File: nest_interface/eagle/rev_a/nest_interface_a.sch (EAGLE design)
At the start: 113 parts, among them J1 MOLEX_MICRO_USB_B_047346, J10 CONN_BLOCK_2, J11 CONN_BLOCK_2, J12 CONN_BLOCK_2, J13 CONN_BLOCK_2, J14 CONN_BLOCK_3, J15 CONN_BLOCK_3, J16 CONN_BLOCK_7, J17 CONN_BLOCK_7, J18 CONN_BLOCK_8, J19 CONN_BLOCK_8, J2 MOLEX_MICRO_USB_B_047346, J20 CONN_BLOCK_8, J21 CONN_BLOCK_8, J5 PJ-036A-SMT, J6 CONN_BLOCK_2, J7 CONN_BLOCK_2, J8 CONN_BLOCK_2, J9 CONN_BLOCK_2, U1 EPIC-CORE_A, U2 MSP430F1611IPM, U3 FT232RL, U4 FT232RL, U5 MPC1825, U6 TC1262, U7 PCA9575, U8 PCA9575, Y1 FC-135_32.768KA-A3

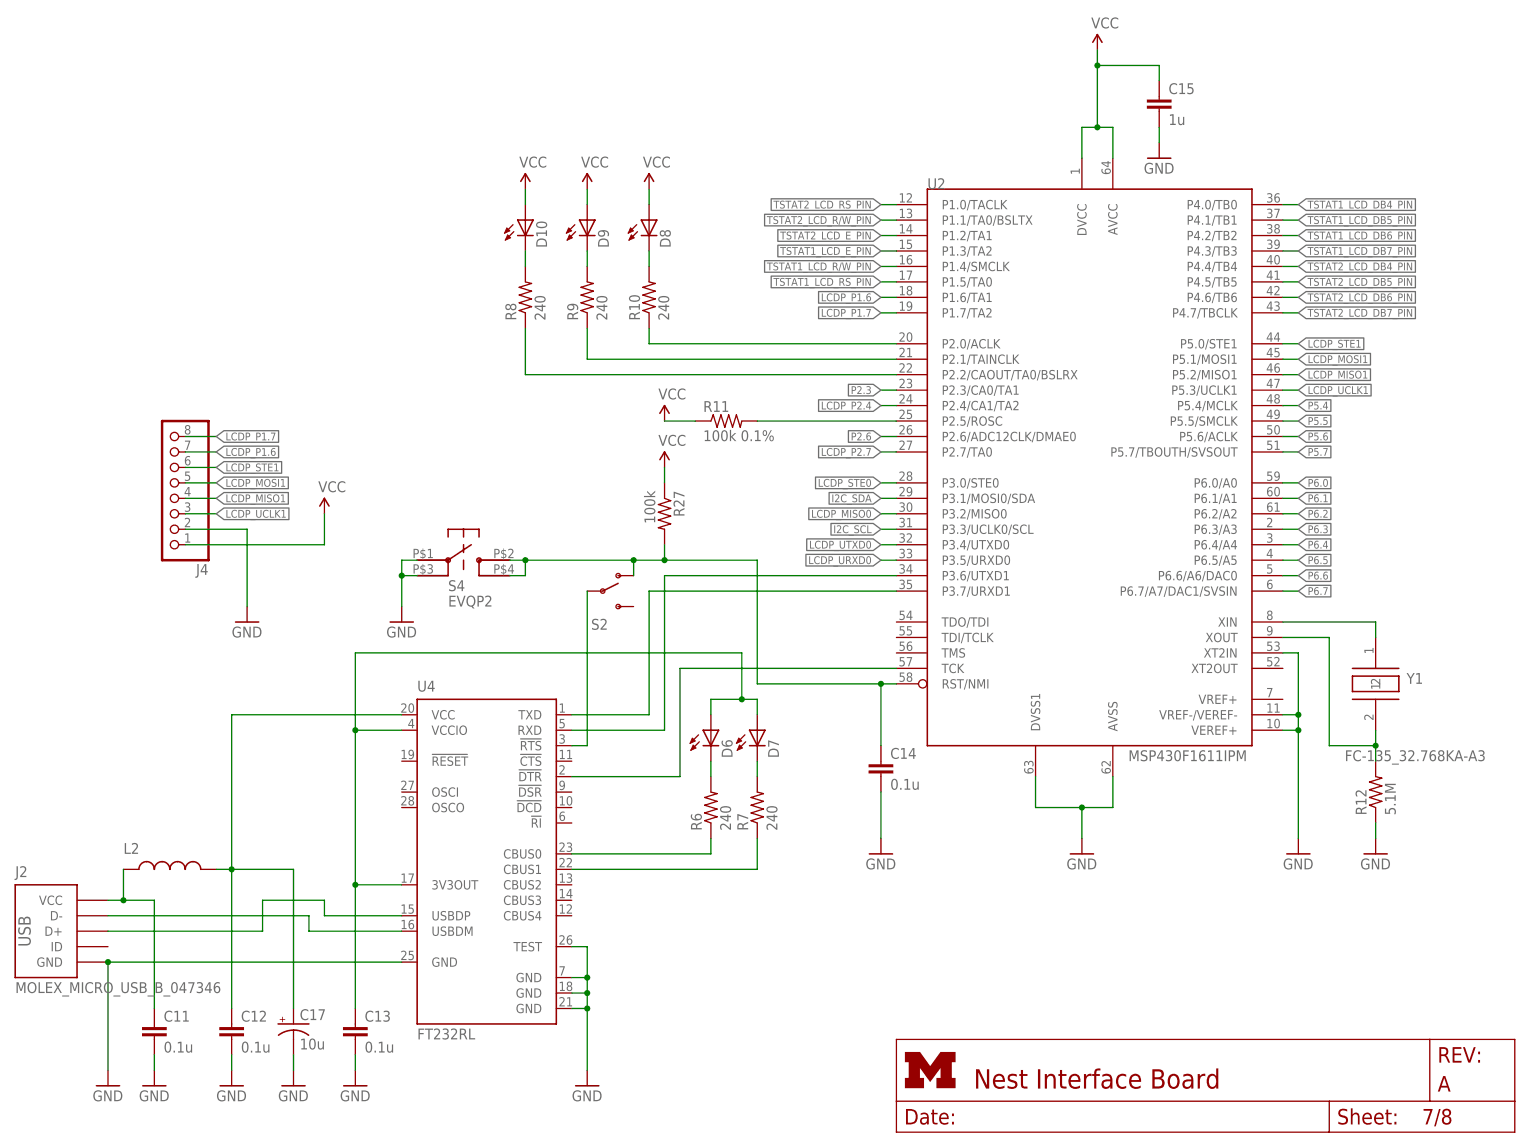
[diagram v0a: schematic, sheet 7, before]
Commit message: added board for keypad socket
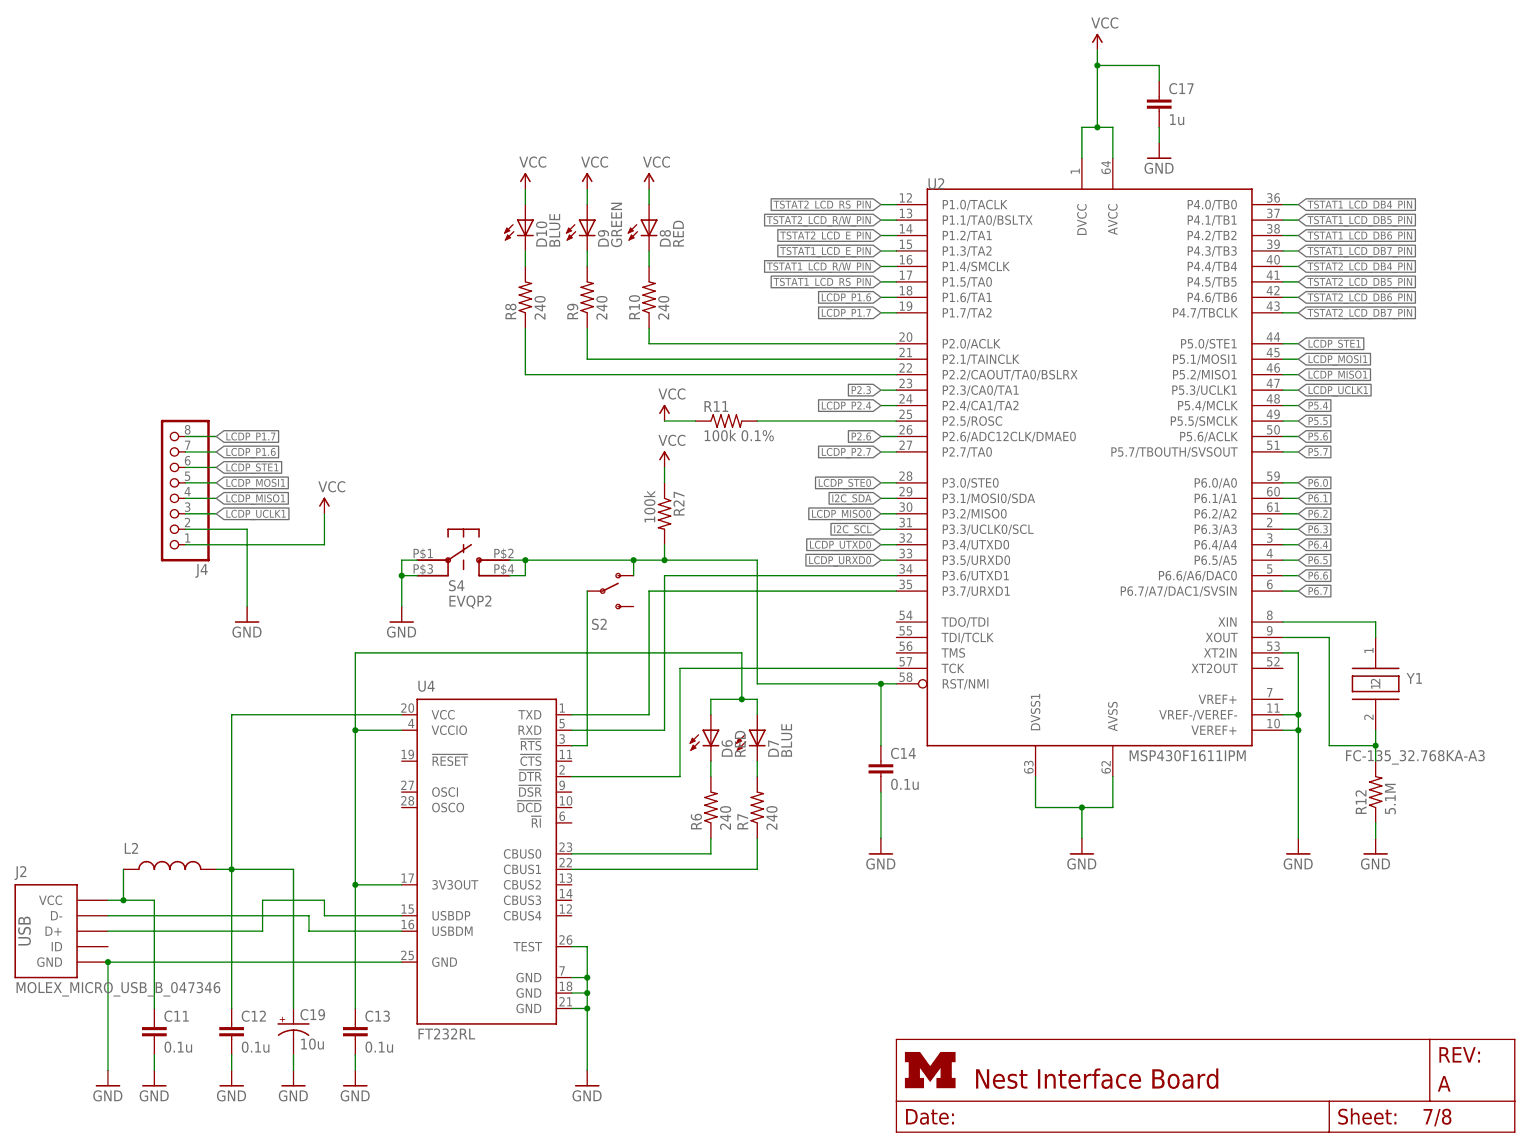
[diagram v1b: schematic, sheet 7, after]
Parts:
- C15: value 1u -> 0.1u
- C16: value 10u -> 0.1u; device SparkFun:CAP_POL1206 -> rcl:C-EUC0603
- C17: value 10u -> 1u; device SparkFun:CAP_POL1206 -> rcl:C-EUC0603
- C18, C19: value 0.1u -> 10u; device rcl:C-EUC0603 -> SparkFun:CAP_POL1206; DIGIKEY (none) -> 478-1655-1-ND
- D1, D3, D6, D8: value (none) -> RED
- D10, D2, D5, D7: value (none) -> BLUE
- D4, D9: value (none) -> GREEN
- L1: DIGIKEY (none) -> 240-2373-1-ND
- S3, S4: DIGIKEY (none) -> P11084SCT-ND
- Y1: DIGIKEY (none) -> 535-9543-1-ND
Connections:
- net GND: now also C16.2, C17.2, C18.-, C19.-; no longer C16.-, C17.-, C18.2, C19.2
- net N$43: now also C19.+; no longer C17.+
- net N$6: now also C18.+; no longer C16.+
- net VCC: now also C16.1, C17.1; no longer C18.1, C19.1

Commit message: nest
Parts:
- removed J4: (no value), pinhead:PINHD-1X8
- added JP1: (no value), pinhead:PINHD-1X10
- added U$1: UMICH_SOLID_LARGE, nest_interface:UMICH_SOLID_LARGE
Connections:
- net P2.3 renamed LCDP_P2.3
- removed net P5.4: U2.P5.4/MCLK
- new net LCDP_P5.4: JP1.2, U2.P5.4/MCLK
- net GND: now also JP1.10; no longer J4.2
- net LCDP_MISO1: now also JP1.5; no longer J4.4
- net LCDP_MOSI1: now also JP1.6; no longer J4.5
- net LCDP_P1.6: now also JP1.8; no longer J4.7
- net LCDP_P1.7: now also JP1.9; no longer J4.8
- net LCDP_P2.4: now also JP1.3
- net LCDP_STE1: now also JP1.7; no longer J4.6
- net LCDP_UCLK1: now also JP1.4; no longer J4.3
- net VCC: now also JP1.1; no longer J4.1
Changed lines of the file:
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@@
 <part name="FRAME7" library="nest_interface" deviceset="LETTER_L" device=""/>
 <part name="FRAME8" library="nest_interface" deviceset="LETTER_L" device=""/>
-<part name="J4" library="pinhead" deviceset="PINHD-1X8" device=""/>
 <part name="GND19" library="supply1" deviceset="GND" device=""/>
 <part name="P+17" library="SparkFun" deviceset="VCC" device=""/>
@@
 <part name="C16" library="rcl" deviceset="C-EU" device="C0603" value="0.1u"/>
 <part name="GND27" library="supply1" deviceset="GND" device=""/>
+<part name="JP1" library="pinhead" deviceset="PINHD-1X10" device=""/>
+<part name="U$1" library="nest_interface" deviceset="UMICH_SOLID" device="_LARGE"/>
 </parts>
 <sheets>
@@
 <instance part="FRAME1" gate="G$1" x="0" y="0"/>
 <instance part="FRAME1" gate="G$2" x="147.32" y="0"/>
+<instance part="U$1" gate="G$1" x="116.84" y="170.18"/>
 </instances>
 <busses>
@@
 <instance part="FRAME7" gate="G$1" x="0" y="0"/>
 <instance part="FRAME7" gate="G$2" x="147.32" y="0"/>
-<instance part="J4" gate="A" x="27.94" y="106.68" rot="R180"/>
-<instance part="GND19" gate="1" x="40.64" y="83.82"/>
-<instance part="P+17" gate="1" x="53.34" y="101.6"/>
+<instance part="GND19" gate="1" x="38.1" y="121.92"/>
+<instance part="P+17" gate="1" x="38.1" y="152.4"/>
+<instance part="JP1" gate="A" x="27.94" y="139.7" rot="MR0"/>
 </instances>
 <busses>
@@
 </segment>
 <segment>
-<pinref part="J4" gate="A" pin="1"/>
-<wire x1="30.48" y1="96.52" x2="53.34" y2="96.52" width="0.1524" layer="91"/>
-<wire x1="53.34" y1="96.52" x2="53.34" y2="101.6" width="0.1524" layer="91"/>
+<pinref part="JP1" gate="A" pin="1"/>
+<wire x1="30.48" y1="149.86" x2="38.1" y2="149.86" width="0.1524" layer="91"/>
 <pinref part="P+17" gate="1" pin="VCC"/>
+<wire x1="38.1" y1="149.86" x2="38.1" y2="152.4" width="0.1524" layer="91"/>
 </segment>
 </net>
@@
 </segment>
 <segment>
-<pinref part="J4" gate="A" pin="2"/>
-<wire x1="30.48" y1="99.06" x2="40.64" y2="99.06" width="0.1524" layer="91"/>
-<wire x1="40.64" y1="99.06" x2="40.64" y2="86.36" width="0.1524" layer="91"/>
+<pinref part="JP1" gate="A" pin="10"/>
+<wire x1="30.48" y1="127" x2="38.1" y2="127" width="0.1524" layer="91"/>
 <pinref part="GND19" gate="1" pin="GND"/>
+<wire x1="38.1" y1="127" x2="38.1" y2="124.46" width="0.1524" layer="91"/>
 </segment>
 </net>
@@
 </segment>
 <segment>
-<pinref part="J4" gate="A" pin="6"/>
-<wire x1="30.48" y1="109.22" x2="35.56" y2="109.22" width="0.1524" layer="91"/>
-<label x="35.56" y="109.22" size="1.27" layer="95" xref="yes"/>
+<pinref part="JP1" gate="A" pin="7"/>
+<wire x1="30.48" y1="134.62" x2="35.56" y2="134.62" width="0.1524" layer="91"/>
+<label x="35.56" y="134.62" size="1.27" layer="95" xref="yes"/>
 </segment>
 </net>
@@
 </segment>
 <segment>
-<pinref part="J4" gate="A" pin="5"/>
-<wire x1="30.48" y1="106.68" x2="35.56" y2="106.68" width="0.1524" layer="91"/>
-<label x="35.56" y="106.68" size="1.27" layer="95" xref="yes"/>
+<pinref part="JP1" gate="A" pin="6"/>
+<wire x1="30.48" y1="137.16" x2="35.56" y2="137.16" width="0.1524" layer="91"/>
+<label x="35.56" y="137.16" size="1.27" layer="95" xref="yes"/>
 </segment>
 </net>
@@
 </segment>
 <segment>
-<pinref part="J4" gate="A" pin="4"/>
-<wire x1="30.48" y1="104.14" x2="35.56" y2="104.14" width="0.1524" layer="91"/>
-<label x="35.56" y="104.14" size="1.27" layer="95" xref="yes"/>
+<pinref part="JP1" gate="A" pin="5"/>
+<wire x1="30.48" y1="139.7" x2="35.56" y2="139.7" width="0.1524" layer="91"/>
+<label x="35.56" y="139.7" size="1.27" layer="95" xref="yes"/>
 </segment>
 </net>
@@
 </segment>
 <segment>
-<pinref part="J4" gate="A" pin="3"/>
-<wire x1="30.48" y1="101.6" x2="35.56" y2="101.6" width="0.1524" layer="91"/>
-<label x="35.56" y="101.6" size="1.27" layer="95" xref="yes"/>
+<pinref part="JP1" gate="A" pin="4"/>
+<wire x1="30.48" y1="142.24" x2="35.56" y2="142.24" width="0.1524" layer="91"/>
+<label x="35.56" y="142.24" size="1.27" layer="95" xref="yes"/>
 </segment>
 </net>
-<net name="P5.4" class="0">
+<net name="LCDP_P5.4" class="0">
 <segment>
 <pinref part="U2" gate="G$1" pin="P5.4/MCLK"/>
@@
 <label x="213.36" y="119.38" size="1.27" layer="95" xref="yes"/>
 </segment>
+<segment>
+<pinref part="JP1" gate="A" pin="2"/>
+<wire x1="30.48" y1="147.32" x2="35.56" y2="147.32" width="0.1524" layer="91"/>
+<label x="35.56" y="147.32" size="1.27" layer="95" xref="yes"/>
+</segment>
 </net>
 <net name="P5.5" class="0">
@@
 </segment>
 <segment>
-<pinref part="J4" gate="A" pin="7"/>
-<wire x1="30.48" y1="111.76" x2="35.56" y2="111.76" width="0.1524" layer="91"/>
-<label x="35.56" y="111.76" size="1.27" layer="95" xref="yes"/>
+<pinref part="JP1" gate="A" pin="8"/>
+<wire x1="30.48" y1="132.08" x2="35.56" y2="132.08" width="0.1524" layer="91"/>
+<label x="35.56" y="132.08" size="1.27" layer="95" xref="yes"/>
 </segment>
 </net>
@@
 </segment>
 <segment>
-<pinref part="J4" gate="A" pin="8"/>
-<wire x1="30.48" y1="114.3" x2="35.56" y2="114.3" width="0.1524" layer="91"/>
-<label x="35.56" y="114.3" size="1.27" layer="95" xref="yes"/>
+<pinref part="JP1" gate="A" pin="9"/>
+<wire x1="30.48" y1="129.54" x2="35.56" y2="129.54" width="0.1524" layer="91"/>
+<label x="35.56" y="129.54" size="1.27" layer="95" xref="yes"/>
 </segment>
 </net>
-<net name="P2.3" class="0">
+<net name="LCDP_P2.3" class="0">
 <segment>
 <pinref part="U2" gate="G$1" pin="P2.3/CA0/TA1"/>
@@
 <label x="144.78" y="119.38" size="1.27" layer="95" rot="R180" xref="yes"/>
 </segment>
+<segment>
+<pinref part="JP1" gate="A" pin="3"/>
+<wire x1="30.48" y1="144.78" x2="35.56" y2="144.78" width="0.1524" layer="91"/>
+<label x="35.56" y="144.78" size="1.27" layer="95" xref="yes"/>
+</segment>
 </net>
